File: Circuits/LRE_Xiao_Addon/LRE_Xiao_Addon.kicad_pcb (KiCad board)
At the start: 2 copper layers, 25 x 25 mm, 14 parts, among them J1 Conn_01x06_Socket, J3 Conn_01x06_Socket, J4 Conn_01x02_Pin, Q1 S8050, Q2 S8050, Q3 S8050

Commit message: PCB update
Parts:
- moved G*** 2.26 mm to (24.3, 29.5)
- moved J4 2.26 mm to (25.8, 29.2)
- moved Q3 1.82 mm to (24.5, 33.2)
- moved R3 1.00 mm to (20.5, 32.5)
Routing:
- net GND: track 59.5 -> 48.2 mm
- net Net-(D5-KG): track 8.19 -> 6.85 mm
- net Net-(Q3-B): track 5.35 -> 4.39 mm
- net Net-(J1-Pin_4): track 11.3 -> 10.6 mm
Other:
- board text added: "V0.4"
- board text removed: "V0.3"
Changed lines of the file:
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@@
 	(footprint "Package_TO_SOT_SMD:SOT-23"
 		(layer "F.Cu")
-		(at 25 34.9375 90)
+		(at 24.5 33.1875 90)
 		(descr "SOT, 3 Pin (https://www.jedec.org/system/files/docs/to-236h.pdf variant AB), generated with kicad-footprint-generator ipc_gullwing_generator.py")
 		(tags "SOT TO_SOT_SMD")
 		(property "Reference" "Q3"
-			(at 2.9375 -1 90)
+			(at -2.8125 0 90)
 			(layer "F.SilkS")
 			(effects
@@
 	(footprint "Resistor_SMD:R_1206_3216Metric_Pad1.30x1.75mm_HandSolder"
 		(layer "F.Cu")
-		(at 20.5 33.55 90)
+		(at 20.5 32.55 90)
 		(descr "Resistor SMD 1206 (3216 Metric), square (rectangular) end terminal, IPC-7351 nominal with elongated pad for handsoldering. (Body size source: IPC-SM-782 page 72, https://www.pcb-3d.com/wordpress/wp-content/uploads/ipc-sm-782a_amendment_1_and_2.pdf), generated with kicad-footprint-generator")
 		(tags "resistor handsolder")
 		(property "Reference" "R3"
-			(at 0 -1.83 90)
+			(at 3.3 0 90)
 			(layer "F.SilkS")
 			(effects
@@
 		(tags "resistor handsolder")
 		(property "Reference" "R6"
-			(at 0 -1.82 90)
+			(at 3.42 0 90)
 			(layer "F.SilkS")
 			(effects
@@
 	(footprint "general:pcbtomo_smol_v2"
 		(layer "B.Cu")
-		(at 24.5 31.75 180)
+		(at 24.275 29.5 180)
 		(property "Reference" "G***"
 			(at 0 0 0)
@@
 	(footprint "Connector_PinHeader_2.54mm:PinHeader_1x02_P2.54mm_Vertical"
 		(layer "B.Cu")
-		(at 26 31.5 90)
+		(at 25.775 29.25 90)
 		(descr "Through hole straight pin header, 1x02, 2.54mm pitch, single row")
 		(tags "Through hole pin header THT 1x02 2.54mm single row")
 		(property "Reference" "J4"
-			(at 2.5 -3.5 90)
+			(at 0.5 2.975 90)
 			(layer "B.SilkS")
 			(effects
@@
 		(attr through_hole)
 		(fp_line
-			(start -1.38 -3.92)
-			(end 1.38 -3.92)
-			(stroke
-				(width 0.12)
-				(type solid)
-			)
-			(layer "B.SilkS")
-		)
-		(fp_line
-			(start 1.38 -1.27)
-			(end 1.38 -3.92)
-			(stroke
-				(width 0.12)
-				(type solid)
-			)
-			(layer "B.SilkS")
-		)
-		(fp_line
-			(start -1.38 -1.27)
-			(end -1.38 -3.92)
-			(stroke
-				(width 0.12)
-				(type solid)
-			)
-			(layer "B.SilkS")
-		)
-		(fp_line
-			(start -1.38 -1.27)
-			(end 1.38 -1.27)
-			(stroke
-				(width 0.12)
-				(type solid)
-			)
-			(layer "B.SilkS")
-		)
-		(fp_line
-			(start -1.38 0)
-			(end -1.38 1.38)
-			(stroke
-				(width 0.12)
-				(type solid)
-			)
-			(layer "B.SilkS")
-		)
-		(fp_line
-			(start -1.38 1.38)
-			(end 0 1.38)
-			(stroke
-				(width 0.12)
-				(type solid)
-			)
-			(layer "B.SilkS")
-		)
-		(fp_line
 			(start 1.77 -4.32)
 			(end 1.77 1.77)
@@
 		)
 	)
-	(gr_text "V0.3"
+	(gr_text "V0.4"
 		(at 13.75 25.75 90)
 		(layer "F.SilkS")
@@
 	)
 	(segment
-		(start 22.8 26.72)
-		(end 24.636 28.556)
+		(start 22.059 29.809)
+		(end 24.5 32.25)
 		(width 0.25)
 		(layer "F.Cu")
@@
 	)
 	(segment
-		(start 24.636 33.636)
-		(end 25 34)
+		(start 22.8 26.72)
+		(end 22.059 27.461)
 		(width 0.25)
 		(layer "F.Cu")
@@
 	)
 	(segment
-		(start 24.636 28.556)
-		(end 24.636 33.636)
+		(start 22.059 27.461)
+		(end 22.059 29.809)
 		(width 0.25)
 		(layer "F.Cu")
@@
 	)
 	(segment
-		(start 24.8865 36.9385)
-		(end 25.95 35.875)
-		(width 0.25)
-		(layer "F.Cu")
-		(net 8)
-	)
-	(segment
 		(start 33 20.96)
 		(end 26.865 14.825)
@@
 	)
 	(segment
-		(start 22.61 30.65)
-		(end 20.003486 30.65)
+		(start 29.256 32.994)
+		(end 31.824 30.426)
 		(width 0.25)
 		(layer "F.Cu")
@@
 	)
 	(segment
-		(start 31.825 22.135)
+		(start 31.824 22.136)
 		(end 33 20.96)
 		(width 0.25)
@@
 	)
 	(segment
-		(start 23.325 14.825)
-		(end 22 16.15)
+		(start 23.235 29.25)
+		(end 26.979 32.994)
 		(width 0.25)
 		(layer "F.Cu")
@@
 	)
 	(segment
-		(start 19.299 31.354486)
-		(end 19.299 32.645514)
-		(width 0.25)
-		(layer "F.Cu")
-		(net 8)
-	)
-	(segment
-		(start 19.629486 32.976)
-		(end 20.51319 32.976)
-		(width 0.25)
-		(layer "F.Cu")
-		(net 8)
-	)
-	(segment
-		(start 23.698678 36.9385)
-		(end 24.8865 36.9385)
+		(start 23.325 14.825)
+		(end 22 16.15)
 		(width 0.25)
 		(layer "F.Cu")
@@
 	)
 	(segment
-		(start 23.424 35.88681)
-		(end 23.424 36.663822)
+		(start 26.581 32.994)
+		(end 25.45 34.125)
 		(width 0.25)
 		(layer "F.Cu")
@@
 	)
 	(segment
-		(start 25.95 35.05)
-		(end 25.95 35.875)
-		(width 0.25)
-		(layer "F.Cu")
-		(net 8)
-	)
-	(segment
-		(start 23.114 31.846)
-		(end 23.46 31.5)
-		(width 0.25)
-		(layer "F.Cu")
-		(net 8)
-	)
-	(segment
-		(start 28.13 32.87)
-		(end 25.95 35.05)
-		(width 0.25)
-		(layer "F.Cu")
-		(net 8)
-	)
-	(segment
-		(start 31.825 30.4651)
-		(end 29.4201 32.87)
-		(width 0.25)
-		(layer "F.Cu")
-		(net 8)
-	)
-	(segment
-		(start 23.46 31.5)
-		(end 22.61 30.65)
+		(start 31.824 30.426)
+		(end 31.824 22.136)
 		(width 0.25)
 		(layer "F.Cu")
@@
 	)
 	(segment
-		(start 19.299 32.645514)
-		(end 19.629486 32.976)
+		(start 26.979 32.994)
+		(end 26.581 32.994)
 		(width 0.25)
 		(layer "F.Cu")
@@
 	)
 	(segment
-		(start 31.825 30.4651)
-		(end 31.825 22.135)
-		(width 0.25)
-		(layer "F.Cu")
-		(net 8)
-	)
-	(segment
-		(start 20.003486 30.65)
-		(end 19.299 31.354486)
-		(width 0.25)
-		(layer "F.Cu")
-		(net 8)
-	)
-	(segment
-		(start 23.424 36.663822)
-		(end 23.698678 36.9385)
-		(width 0.25)
-		(layer "F.Cu")
-		(net 8)
-	)
-	(segment
-		(start 20.51319 32.976)
-		(end 23.424 35.88681)
-		(width 0.25)
-		(layer "F.Cu")
-		(net 8)
-	)
-	(segment
-		(start 29.4201 32.87)
-		(end 28.13 32.87)
+		(start 29.256 32.994)
+		(end 26.979 32.994)
 		(width 0.25)
 		(layer "F.Cu")
@@
 	)
 	(segment
-		(start 20.5 32.325)
-		(end 20.5 32)
+		(start 20.5 31.075)
+		(end 23.55 34.125)
 		(width 0.25)
 		(layer "F.Cu")
@@
 	)
 	(segment
-		(start 24.05 35.875)
-		(end 20.5 32.325)
+		(start 20.5 31)
+		(end 20.5 31.075)
 		(width 0.25)
 		(layer "F.Cu")
@@
 	)
 	(segment
-		(start 19.625 35.1)
-		(end 20.5 35.1)
+		(start 18.625 34.1)
+		(end 16.324 31.799)
 		(width 0.25)
 		(layer "F.Cu")
@@
 	)
 	(segment
-		(start 16.324 31.799)
-		(end 19.625 35.1)
+		(start 20.5 34.1)
+		(end 18.625 34.1)
 		(width 0.25)
 		(layer "F.Cu")
@@
 	(segment
 		(start 17.5 26.04)
-		(end 19.5 28.04)
+		(end 17.54 26.04)
 		(width 0.25)
 		(layer "F.Cu")
@@
 	)
 	(segment
-		(start 19.5 28.04)
-		(end 19.5 29)
+		(start 17.54 26.04)
+		(end 20.75 29.25)
 		(width 0.25)
 		(layer "F.Cu")
@@
 	)
 	(via
-		(at 19.5 29)
+		(at 20.75 29.25)
 		(size 0.8)
 		(drill 0.4)
@@
 	)
 	(segment
-		(start 23.5 29)
-		(end 26 31.5)
+		(start 21.926 30.426)
+		(end 24.599 30.426)
+		(width 0.25)
+		(layer "B.Cu")
+		(net 14)
+	)
+	(segment
+		(start 20.75 29.25)
+		(end 21.926 30.426)
 		(width 0.25)
 		(layer "B.Cu")
@@
 	)
 	(segment
-		(start 19.5 29)
-		(end 23.5 29)
+		(start 24.599 30.426)
+		(end 25.775 29.25)
 		(width 0.25)
 		(layer "B.Cu")

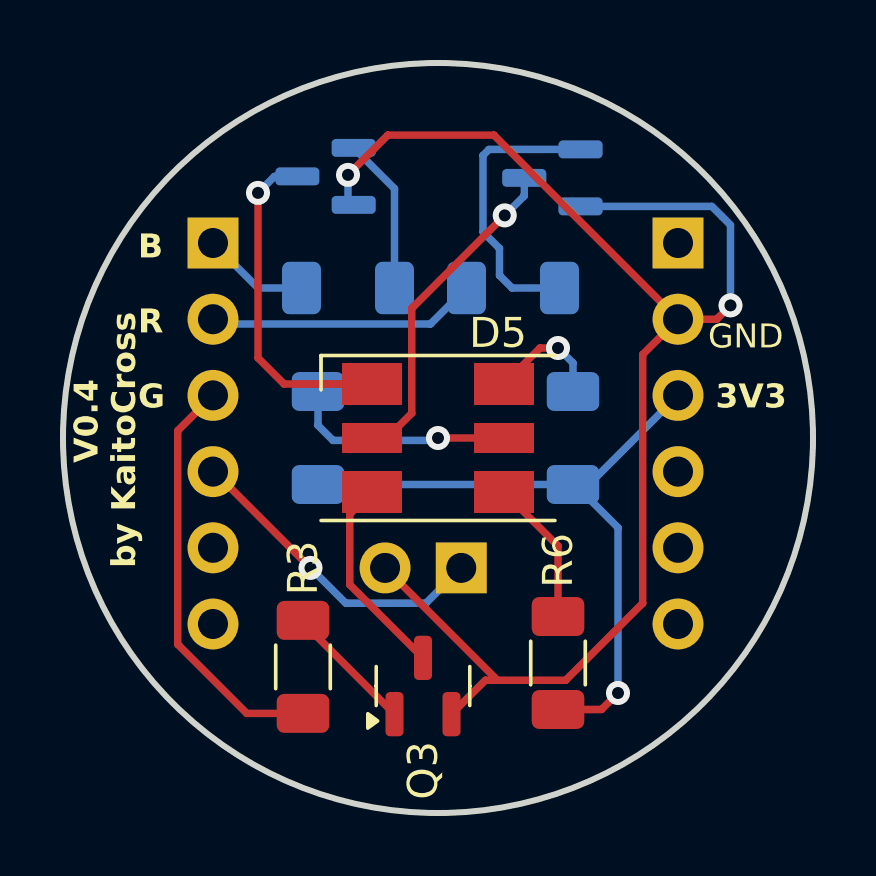
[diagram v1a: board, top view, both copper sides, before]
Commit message: PCB changes: RGB Pins moved, voltage div to A0 for measuring batt voltage, voltage div to detect VBUS voltage
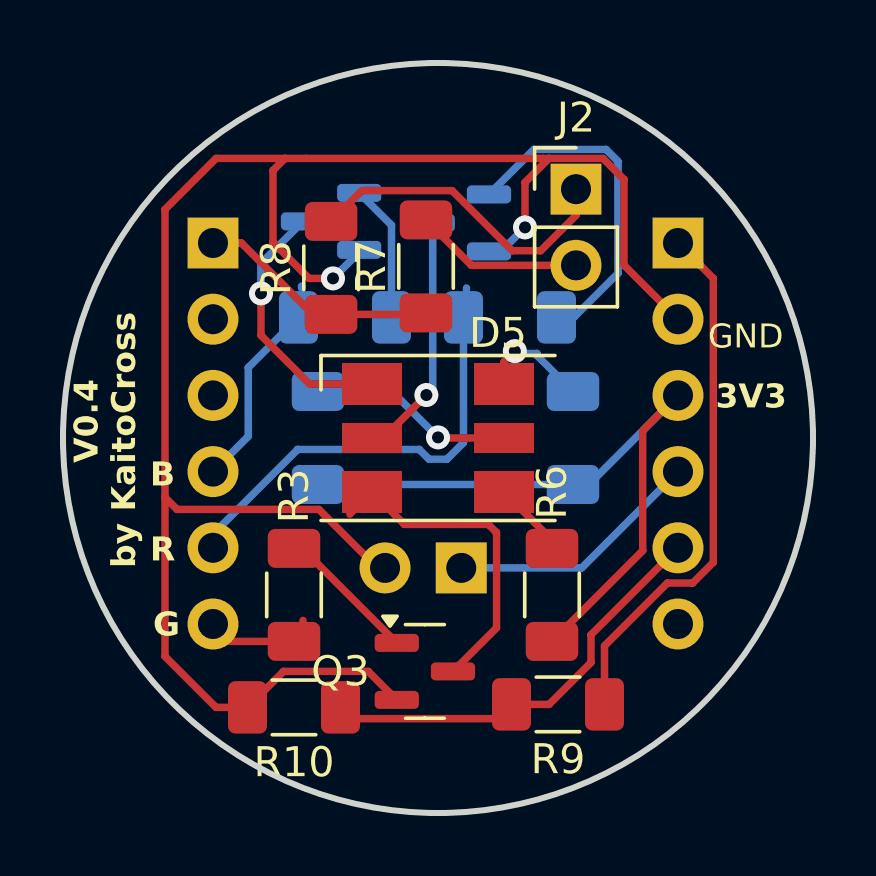
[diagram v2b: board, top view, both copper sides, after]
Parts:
- added J2: Conn_01x02_Pin, Connector_PinHeader_2.54mm:PinHeader_1x02_P2.54mm_Vertical, F.Cu at (29.6, 16.6)
- added R10: 10000, Resistor_SMD:R_1206_3216Metric_Pad1.30x1.75mm_HandSolder, F.Cu at (20.2, 33.9)
- added R7: 270000, Resistor_SMD:R_1206_3216Metric_Pad1.30x1.75mm_HandSolder, F.Cu at (24.6, 19.2)
- added R8: 270000, Resistor_SMD:R_1206_3216Metric_Pad1.30x1.75mm_HandSolder, F.Cu at (21.4, 19.2)
- added R9: 6666, Resistor_SMD:R_1206_3216Metric_Pad1.30x1.75mm_HandSolder, F.Cu at (29.0, 33.8)
- R5: value 40 -> 65
- moved Q2 3.40 mm to (25.8, 17.8)
- moved R3 2.42 mm to (20.2, 30.1)
- moved R6 2.28 mm to (28.8, 30.1)
- moved Q1 1.51 mm to (21.4, 17.7)
- moved R1 0.99 mm to (21.9, 20.9)
- moved R2 0.99 mm to (27.4, 20.9)
- moved Q3 0.49 mm to (24.6, 32.7), turned to 0 degrees
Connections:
- J1 pad 2: Net-(J1-Pin_2) -> unconnected-(J1-Pin_2-Pad2)
- J1 pad 3: Net-(J1-Pin_3) -> unconnected-(J1-Pin_3-Pad3)
- J1 pad 5: unconnected-(J1-Pin_5-Pad5) -> Net-(J1-Pin_5)
- J1 pad 6: unconnected-(J1-Pin_6-Pad6) -> Net-(J1-Pin_6)
- J3 pad 1: unconnected-(J3-Pin_1-Pad1) -> Net-(J3-Pin_1)
- J3 pad 4: unconnected-(J3-Pin_4-Pad4) -> Net-(J3-Pin_4)
- J3 pad 5: unconnected-(J3-Pin_5-Pad5) -> Net-(J3-Pin_5)
- J4 pad 1: Net-(J1-Pin_4) -> Net-(J3-Pin_4)
- R1 pad 1: Net-(J1-Pin_1) -> Net-(J1-Pin_4)
- R2 pad 1: Net-(J1-Pin_2) -> Net-(J1-Pin_5)
- R3 pad 1: Net-(J1-Pin_3) -> Net-(J1-Pin_6)
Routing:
- net Net-(J3-Pin_1): track 0.00 -> 17.9 mm
- net GND: track 48.2 -> 65.2 mm
- net Net-(J1-Pin_5): track 0.00 -> 14.8 mm
- net Net-(J3-Pin_5): track 0.00 -> 14.3 mm
- net Net-(J1-Pin_3): track 13.9 -> 0.00 mm
- net Net-(J2-Pin_1): track 0.00 -> 10.8 mm
- net Net-(J1-Pin_2): track 9.08 -> 0.00 mm
- net Net-(J3-Pin_4): track 0.00 -> 8.55 mm
- net Net-(J2-Pin_2): track 0.00 -> 5.63 mm
- net Net-(J1-Pin_1): track 3.63 -> 8.11 mm
- net Net-(J1-Pin_4): track 10.6 -> 6.42 mm, vias 1 -> 0
- net Net-(D5-KG): track 6.85 -> 11.0 mm
- net Net-(J1-Pin_6): track 0.00 -> 3.02 mm
- net Net-(D5-KB): track 11.2 -> 8.75 mm
- net Net-(D5-AG): track 4.90 -> 2.54 mm
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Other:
- board text added: "${REFERENCE}"
